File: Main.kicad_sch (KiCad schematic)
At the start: 5 parts, among them J2 U, J3 V, J4 W, J5 U, J6 V

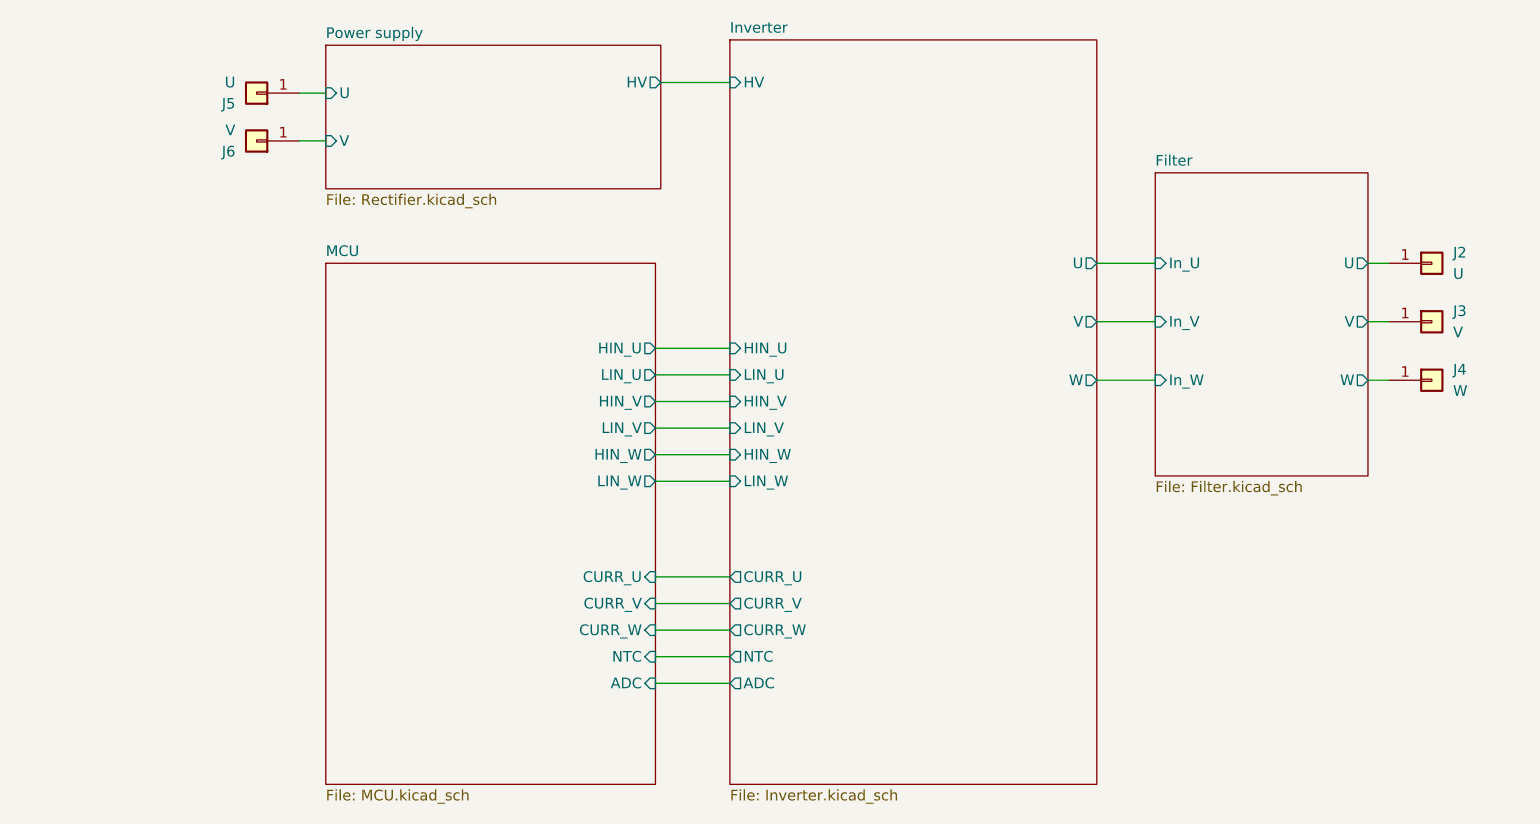
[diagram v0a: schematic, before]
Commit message: update power supply page
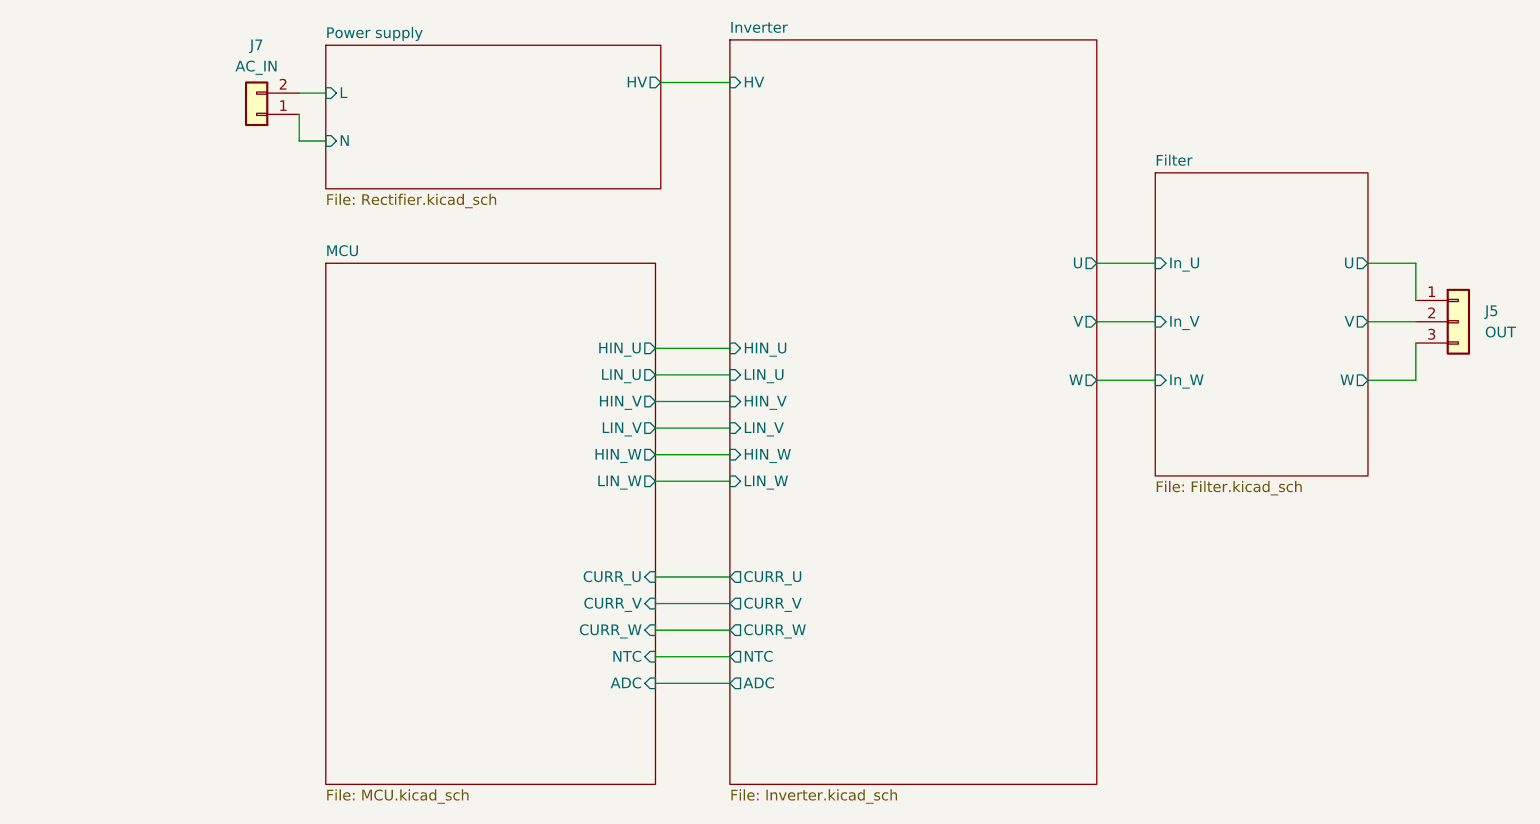
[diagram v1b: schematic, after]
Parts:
- removed J2, J5: U, symbol Connector_Generic:Conn_01x01
- removed J3, J6: V, symbol Connector_Generic:Conn_01x01
- removed J4: W, symbol Connector_Generic:Conn_01x01
- added J5: OUT, symbol Connector_Generic:Conn_01x03
- added J7: AC_IN, symbol Connector_Generic:Conn_01x02
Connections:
- net Filter/U: now also J5.1 (Pin_1)
- net Filter/V: now also J5.2 (Pin_2)
- net Filter/W: now also J5.3 (Pin_3)
- new net Power supply/L: J7.2 (Pin_2)
- new net Power supply/N: J7.1 (Pin_1)
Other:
- sheet Power supply ports: added L, N; removed U, V
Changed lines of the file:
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@@
 (kicad_sch (version 20230121) (generator eeschema)
   (paper "A4")
-  (wire (pts (xy 210.82 85.725) (xy 213.36 85.725))
+  (wire (pts (xy 210.82 85.725) (xy 216.535 85.725))
     (stroke (width 0) (type default))
   )
@@
     (stroke (width 0) (type default))
   )
-  (wire (pts (xy 210.82 71.755) (xy 213.36 71.755))
+  (wire (pts (xy 210.82 71.755) (xy 216.535 71.755))
     (stroke (width 0) (type default))
   )
@@
     (stroke (width 0) (type default))
   )
+  (wire (pts (xy 216.535 81.28) (xy 216.535 85.725))
+    (stroke (width 0) (type default))
+  )
   (wire (pts (xy 125.73 91.44) (xy 134.62 91.44))
     (stroke (width 0) (type default))
   )
   (wire (pts (xy 125.73 109.22) (xy 134.62 109.22))
+    (stroke (width 0) (type default))
+  )
+  (wire (pts (xy 83.185 53.975) (xy 83.185 57.15))
     (stroke (width 0) (type default))
   )
@@
     (stroke (width 0) (type default))
   )
-  (wire (pts (xy 210.82 78.74) (xy 213.36 78.74))
+  (wire (pts (xy 210.82 78.74) (xy 216.535 78.74))
+    (stroke (width 0) (type default))
+  )
+  (wire (pts (xy 216.535 71.755) (xy 216.535 76.2))
     (stroke (width 0) (type default))
   )
@@
     (stroke (width 0) (type default))
   )
-  (symbol (lib_id "Connector_Generic:Conn_01x01") (at 218.44 85.725 0) (unit 1)
+  (symbol (lib_id "Connector_Generic:Conn_01x03") (at 221.615 78.74 0) (unit 1)
     (in_bom yes) (on_board yes) (dnp no) (fields_autoplaced)
-    (property "Reference" "J4" (at 220.98 84.455 0)
+    (property "Reference" "J5" (at 224.79 77.47 0)
       (effects (font (size 1.27 1.27)) (justify left))
     )
-    (property "Value" "W" (at 220.98 86.995 0)
+    (property "Value" "OUT" (at 224.79 80.01 0)
       (effects (font (size 1.27 1.27)) (justify left))
     )
-    (property "Footprint" "" (at 218.44 85.725 0)
+    (property "Footprint" "" (at 221.615 78.74 0)
       (effects (font (size 1.27 1.27)) hide)
     )
-    (property "Datasheet" "~" (at 218.44 85.725 0)
+    (property "Datasheet" "~" (at 221.615 78.74 0)
       (effects (font (size 1.27 1.27)) hide)
     )
     (pin "1")
-    (instances
-      (project "Main"
-        (path "/c97a22ab-71f8-4b91-b313-15b8a3e640d7"
-          (reference "J4") (unit 1)
-        )
-      )
-    )
-  )
-  (symbol (lib_id "Connector_Generic:Conn_01x01") (at 78.105 51.435 180) (unit 1)
-    (in_bom yes) (on_board yes) (dnp no) (fields_autoplaced)
-    (property "Reference" "J5" (at 75.565 52.705 0)
-      (effects (font (size 1.27 1.27)) (justify left))
-    )
-    (property "Value" "U" (at 75.565 50.165 0)
-      (effects (font (size 1.27 1.27)) (justify left))
-    )
-    (property "Footprint" "" (at 78.105 51.435 0)
-      (effects (font (size 1.27 1.27)) hide)
-    )
-    (property "Datasheet" "~" (at 78.105 51.435 0)
-      (effects (font (size 1.27 1.27)) hide)
-    )
-    (pin "1")
+    (pin "2")
+    (pin "3")
     (instances
       (project "Main"
@@
     )
   )
-  (symbol (lib_id "Connector_Generic:Conn_01x01") (at 218.44 78.74 0) (unit 1)
+  (symbol (lib_id "Connector_Generic:Conn_01x02") (at 78.105 53.975 180) (unit 1)
     (in_bom yes) (on_board yes) (dnp no) (fields_autoplaced)
-    (property "Reference" "J3" (at 220.98 77.47 0)
-      (effects (font (size 1.27 1.27)) (justify left))
+    (property "Reference" "J7" (at 78.105 45.72 0)
+      (effects (font (size 1.27 1.27)))
     )
-    (property "Value" "V" (at 220.98 80.01 0)
-      (effects (font (size 1.27 1.27)) (justify left))
+    (property "Value" "AC_IN" (at 78.105 48.26 0)
+      (effects (font (size 1.27 1.27)))
     )
-    (property "Footprint" "" (at 218.44 78.74 0)
+    (property "Footprint" "" (at 78.105 53.975 0)
       (effects (font (size 1.27 1.27)) hide)
     )
-    (property "Datasheet" "~" (at 218.44 78.74 0)
+    (property "Datasheet" "~" (at 78.105 53.975 0)
       (effects (font (size 1.27 1.27)) hide)
     )
     (pin "1")
+    (pin "2")
     (instances
       (project "Main"
         (path "/c97a22ab-71f8-4b91-b313-15b8a3e640d7"
-          (reference "J3") (unit 1)
-        )
-      )
-    )
-  )
-  (symbol (lib_id "Connector_Generic:Conn_01x01") (at 78.105 57.15 180) (unit 1)
-    (in_bom yes) (on_board yes) (dnp no)
-    (property "Reference" "J6" (at 75.565 58.42 0)
-      (effects (font (size 1.27 1.27)) (justify left))
-    )
-    (property "Value" "V" (at 75.565 55.88 0)
-      (effects (font (size 1.27 1.27)) (justify left))
-    )
-    (property "Footprint" "" (at 78.105 57.15 0)
-      (effects (font (size 1.27 1.27)) hide)
-    )
-    (property "Datasheet" "~" (at 78.105 57.15 0)
-      (effects (font (size 1.27 1.27)) hide)
-    )
-    (pin "1")
-    (instances
-      (project "Main"
-        (path "/c97a22ab-71f8-4b91-b313-15b8a3e640d7"
-          (reference "J6") (unit 1)
-        )
-      )
-    )
-  )
-  (symbol (lib_id "Connector_Generic:Conn_01x01") (at 218.44 71.755 0) (unit 1)
-    (in_bom yes) (on_board yes) (dnp no) (fields_autoplaced)
-    (property "Reference" "J2" (at 220.98 70.485 0)
-      (effects (font (size 1.27 1.27)) (justify left))
-    )
-    (property "Value" "U" (at 220.98 73.025 0)
-      (effects (font (size 1.27 1.27)) (justify left))
-    )
-    (property "Footprint" "" (at 218.44 71.755 0)
-      (effects (font (size 1.27 1.27)) hide)
-    )
-    (property "Datasheet" "~" (at 218.44 71.755 0)
-      (effects (font (size 1.27 1.27)) hide)
-    )
-    (pin "1")
-    (instances
-      (project "Main"
-        (path "/c97a22ab-71f8-4b91-b313-15b8a3e640d7"
-          (reference "J2") (unit 1)
+          (reference "J7") (unit 1)
         )
       )
@@
       (effects (font (size 1.27 1.27)) (justify left top))
     )
-    (pin "U" input (at 86.36 51.435 180)
-      (effects (font (size 1.27 1.27)) (justify left))
-    )
-    (pin "V" input (at 86.36 57.15 180)
-      (effects (font (size 1.27 1.27)) (justify left))
-    )
     (pin "HV" output (at 126.365 50.165 0)
       (effects (font (size 1.27 1.27)) (justify right))
     )
+    (pin "L" input (at 86.36 51.435 180)
+      (effects (font (size 1.27 1.27)) (justify left))
+    )
+    (pin "N" input (at 86.36 57.15 180)
+      (effects (font (size 1.27 1.27)) (justify left))
+    )
     (instances

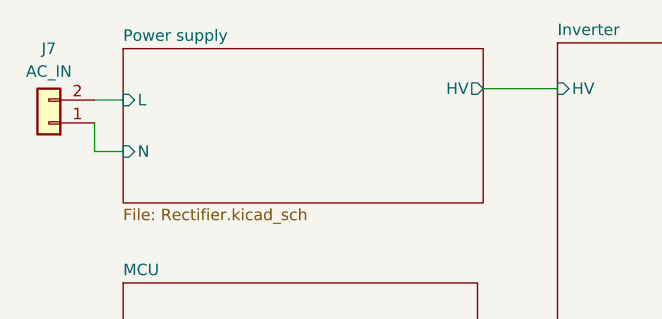
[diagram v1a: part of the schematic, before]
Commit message: update power label
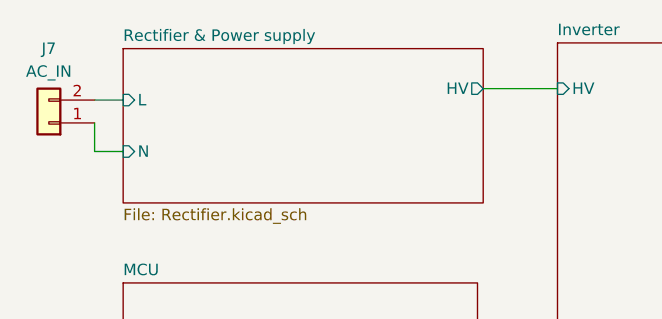
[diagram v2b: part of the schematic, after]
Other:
- sheet Power supply renamed Rectifier & Power supply
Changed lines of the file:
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@@
     (stroke (width 0.1524) (type solid))
     (fill (color 0 0 0 0.0000))
-    (property "Sheetname" "Power supply" (at 86.36 45.0084 0)
+    (property "Sheetname" "Rectifier & Power supply" (at 86.36 45.0084 0)
       (effects (font (size 1.27 1.27)) (justify left bottom))
     )
